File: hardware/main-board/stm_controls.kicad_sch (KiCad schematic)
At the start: 57 parts, among them J10 USB_C_Receptacle_USB2.0_14P, J11 Conn_02x05_Odd_Even, J12 Conn_01x02_Pin, J13 Conn_01x02_Pin, SW3 SW_SPST, SW4 SW_SPST, U1 CD22M3494MQZ, U11 CD22M3494MQZ, U12 CD22M3494MQZ, U14 AD5263BRUZ200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

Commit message: The PCB is coming together
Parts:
- J12, J13: footprint Connector_PinHeader_1.00mm:PinHeader_1x02_P1.00mm_Horizontal -> Connector_PinSocket_2.54mm:PinSocket_1x02_P2.54mm_Vertical
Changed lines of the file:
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@@
 			)
 		)
-		(property "Footprint" "Connector_PinHeader_1.00mm:PinHeader_1x02_P1.00mm_Horizontal"
+		(property "Footprint" "Connector_PinSocket_2.54mm:PinSocket_1x02_P2.54mm_Vertical"
 			(at 194.31 96.52 0)
 			(effects
@@
 			)
 		)
-		(property "Footprint" "Connector_PinHeader_1.00mm:PinHeader_1x02_P1.00mm_Horizontal"
+		(property "Footprint" "Connector_PinSocket_2.54mm:PinSocket_1x02_P2.54mm_Vertical"
 			(at 194.31 111.76 0)
 			(effects

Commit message: Added wiring to cells and compacted input
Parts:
- J11: footprint Connector_PinHeader_1.00mm:PinHeader_2x05_P1.00mm_Horizontal -> Connector_PinHeader_2.54mm:PinHeader_2x05_P2.54mm_Vertical
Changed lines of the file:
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@@
 			)
 		)
-		(property "Footprint" "Connector_PinHeader_1.00mm:PinHeader_2x05_P1.00mm_Horizontal"
+		(property "Footprint" "Connector_PinHeader_2.54mm:PinHeader_2x05_P2.54mm_Vertical"
 			(at 191.77 135.89 0)
 			(effects

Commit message: feat: Part nos plus some micro fixup
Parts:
- C20, C23, C24, C25, C26, C27: DKPN (none) -> C0603C104K5RACTU
- C21, C22: DKPN (none) -> LMK107BBJ106MALT
- C28: DKPN (none) -> C0603C103K5RACTU
- C29, C30: DKPN (none) -> C0603C105K4RACTU
- D10, D14: DKPN (none) -> LG R971-KN-1-0-20-R18
- D11: value D_Schottky -> BAT60JFILM; footprint Diode_SMD:D_SOD-123 -> Diode_SMD:D_SOD-323_HandSoldering; DKPN (none) -> BAT60JFILM
- D12: DKPN (none) -> QBLP631-IB5-2897
- D13, D9: DKPN (none) -> LS R976-NR-1-0-20-R18
- FB1: DKPN (none) -> BLM18PG121SN1D
- R2: value 5.1kΩ -> 5.1k
- R3: value R_US -> 5.1k
- SW3, SW4: footprint Button_Switch_SMD:SW_SPST_B3U-1100P -> Button_Switch_SMD:SW_SPST_SKQG_WithoutStem; DKPN (none) -> SKQGABE010
- U1, U11, U12, U17, U18, U23, U24, U29, U30: MPN (none) -> 968-CD22M3494MQZ
- U14, U15, U20, U21, U26, U27, U8, U9: DKPN (none) -> AD5263BRUZ200-R7; MPN AD5263BRUZ200 -> (none)
- U34, U36, U38: DKPN (none) -> 74HC164D
- U35: DKPN (none) -> FT232RNL-TUBE
- U37: DKPN (none) -> STM32F091RC

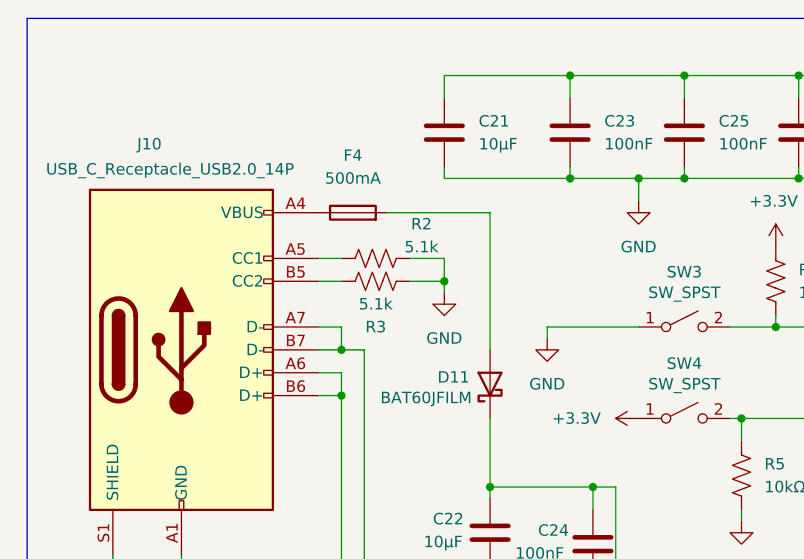
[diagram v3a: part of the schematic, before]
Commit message: finalized component list, fixed DRC errors
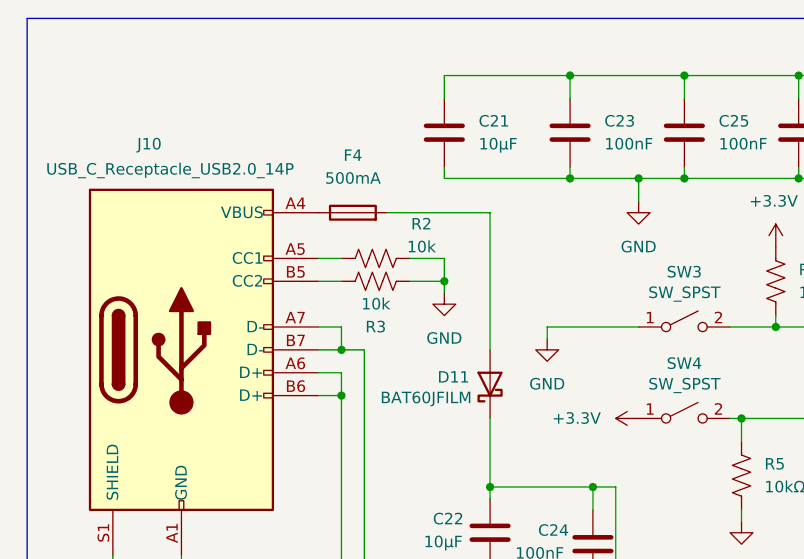
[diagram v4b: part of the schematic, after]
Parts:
- F4: DKPN (none) -> C2Q500
- J10: DKPN (none) -> 1003-030-01210-TR
- R1, R10, R4, R6, R9: DKPN (none) -> ERA-3AEB151V
- R2, R3: value 5.1k -> 10k; DKPN (none) -> ESR03EZPF1002
- R5, R7, R8: DKPN (none) -> ESR03EZPF1002
- U1, U11, U12, U17, U18, U23, U24, U29, U30: DKPN (none) -> CD22M3494MQZ
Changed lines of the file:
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@@
 			)
 		)
+		(property "DKPN" "ESR03EZPF1002"
+			(at 109.22 109.22 0)
+			(effects
+				(font
+					(size 1.27 1.27)
+				)
+				(hide yes)
+			)
+		)
 		(pin "2"
 		)
@@
 			)
 		)
-		(property "Value" "5.1k"
+		(property "Value" "10k"
 			(at 66.04 38.1 90)
 			(effects
@@
 			)
 		)
+		(property "DKPN" "ESR03EZPF1002"
+			(at 60.96 39.37 90)
+			(effects
+				(font
+					(size 1.27 1.27)
+				)
+				(hide yes)
+			)
+		)
 		(pin "1"
 		)
@@
 			)
 		)
+		(property "DKPN" "CD22M3494MQZ"
+			(at 336.55 116.84 0)
+			(effects
+				(font
+					(size 1.27 1.27)
+				)
+				(hide yes)
+			)
+		)
 		(pin "6"
 		)
@@
 			)
 		)
+		(property "DKPN" "CD22M3494MQZ"
+			(at 293.37 60.96 0)
+			(effects
+				(font
+					(size 1.27 1.27)
+				)
+				(hide yes)
+			)
+		)
 		(pin "6"
 		)
@@
 			)
 		)
+		(property "DKPN" "CD22M3494MQZ"
+			(at 336.55 88.9 0)
+			(effects
+				(font
+					(size 1.27 1.27)
+				)
+				(hide yes)
+			)
+		)
 		(pin "6"
 		)
@@
 			)
 		)
+		(property "DKPN" "ERA-3AEB151V"
+			(at 66.04 236.22 0)
+			(effects
+				(font
+					(size 1.27 1.27)
+				)
+				(hide yes)
+			)
+		)
 		(pin "1"
 		)
@@
 			)
 		)
+		(property "DKPN" "CD22M3494MQZ"
+			(at 293.37 88.9 0)
+			(effects
+				(font
+					(size 1.27 1.27)
+				)
+				(hide yes)
+			)
+		)
 		(pin "6"
 		)
@@
 			)
 		)
+		(property "DKPN" "CD22M3494MQZ"
+			(at 293.37 116.84 0)
+			(effects
+				(font
+					(size 1.27 1.27)
+				)
+				(hide yes)
+			)
+		)
 		(pin "6"
 		)
@@
 			)
 		)
+		(property "DKPN" "CD22M3494MQZ"
+			(at 250.19 88.9 0)
+			(effects
+				(font
+					(size 1.27 1.27)
+				)
+				(hide yes)
+			)
+		)
 		(pin "6"
 		)
@@
 			)
 		)
-		(property "Value" "5.1k"
+		(property "Value" "10k"
 			(at 60.96 44.45 90)
 			(effects
@@
 			)
 		)
+		(property "DKPN" "ESR03EZPF1002"
+			(at 60.96 41.91 90)
+			(effects
+				(font
+					(size 1.27 1.27)
+				)
+				(hide yes)
+			)
+		)
 		(pin "1"
 		)
@@
 			)
 		)
+		(property "DKPN" "CD22M3494MQZ"
+			(at 250.19 60.96 0)
+			(effects
+				(font
+					(size 1.27 1.27)
+				)
+				(hide yes)
+			)
+		)
 		(pin "6"
 		)
@@
 			)
 		)
+		(property "DKPN" "ESR03EZPF1002"
+			(at 101.6 63.5 0)
+			(effects
+				(font
+					(size 1.27 1.27)
+				)
+				(hide yes)
+			)
+		)
 		(pin "1"
 		)
@@
 			)
 		)
+		(property "DKPN" "CD22M3494MQZ"
+			(at 336.55 60.96 0)
+			(effects
+				(font
+					(size 1.27 1.27)
+				)
+				(hide yes)
+			)
+		)
 		(pin "6"
 		)
@@
 			)
 		)
+		(property "DKPN" "ERA-3AEB151V"
+			(at 39.37 236.22 0)
+			(effects
+				(font
+					(size 1.27 1.27)
+				)
+				(hide yes)
+			)
+		)
 		(pin "1"
 		)
@@
 			)
 		)
+		(property "DKPN" "CD22M3494MQZ"
+			(at 250.19 116.84 0)
+			(effects
+				(font
+					(size 1.27 1.27)
+				)
+				(hide yes)
+			)
+		)
 		(pin "6"
 		)
@@
 			)
 		)
+		(property "DKPN" "1003-030-01210-TR"
+			(at 39.37 49.53 0)
+			(effects
+				(font
+					(size 1.27 1.27)
+				)
+				(hide yes)
+			)
+		)
 		(pin "S1"
 		)
@@
 		(instances
 			(project ""
+				(path "/5dd933ff-bc57-4741-8957-85d8c6e75130/534f316e-b737-411c-8d6f-20e6ab703659"
+					(reference "J10")
+					(unit 1)
+				)
 				(path "/5dd933ff-bc57-4741-8957-85d8c6e75130/72af25e1-7cdc-412a-8304-78174a178e92"
 					(reference "J10")
@@
 			)
 		)
+		(property "DKPN" "ERA-3AEB151V"
+			(at 101.6 234.95 0)
+			(effects
+				(font
+					(size 1.27 1.27)
+				)
+				(hide yes)
+			)
+		)
 		(pin "1"
 		)
@@
 			)
 		)
+		(property "DKPN" "ESR03EZPF1002"
+			(at 105.41 41.91 0)
+			(effects
+				(font
+					(size 1.27 1.27)
+				)
+				(hide yes)
+			)
+		)
 		(pin "1"
 		)
@@
 			)
 		)
+		(property "DKPN" "C2Q500"
+			(at 58.42 34.29 90)
+			(effects
+				(font
+					(size 1.27 1.27)
+				)
+				(hide yes)
+			)
+		)
 		(pin "2"
 		)
@@
 			)
 		)
+		(property "DKPN" "ERA-3AEB151V"
+			(at 137.16 234.95 0)
+			(effects
+				(font
+					(size 1.27 1.27)
+				)
+				(hide yes)
+			)
+		)
 		(pin "1"
 		)
@@
 			(at 120.65 234.95 0)
 			(effects
+				(font
+					(size 1.27 1.27)
+				)
+				(hide yes)
+			)
+		)
+		(property "DKPN" "ERA-3AEB151V"
+			(at 120.65 234.95 0)
+			(effects
